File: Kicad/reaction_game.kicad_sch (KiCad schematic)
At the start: 11 parts, among them SW1 Player 1, SW2 Player 2, U1 RaspberryPico

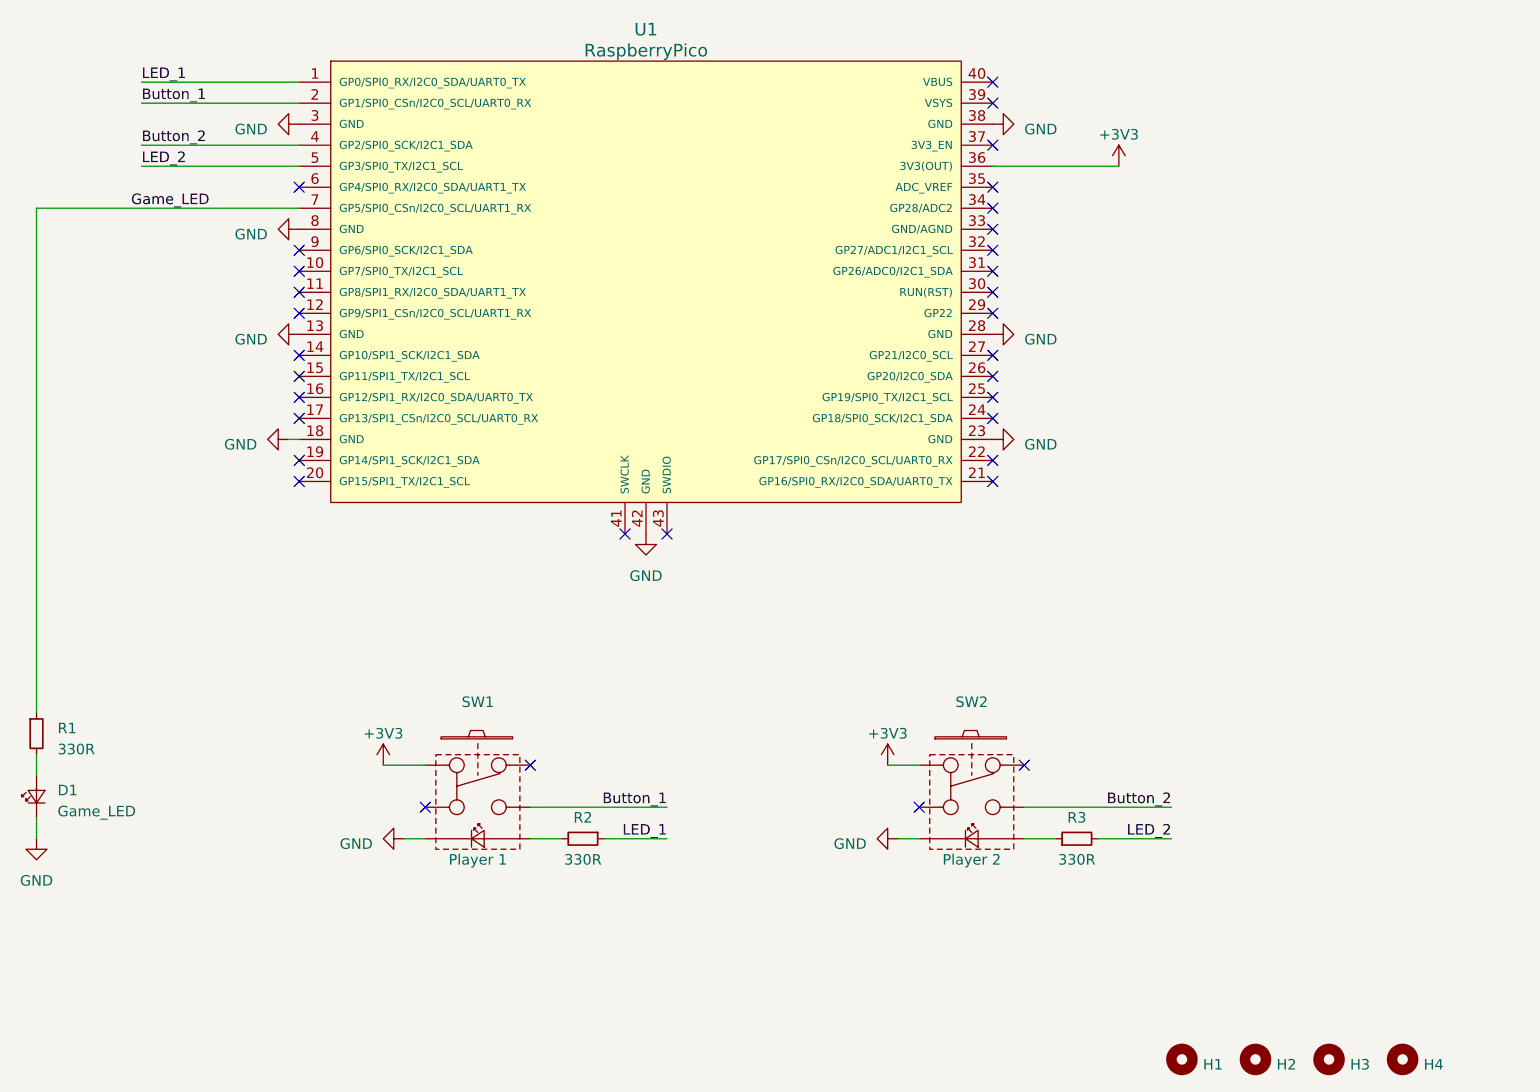
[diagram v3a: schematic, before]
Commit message: Fixed Pico
- flipped pico
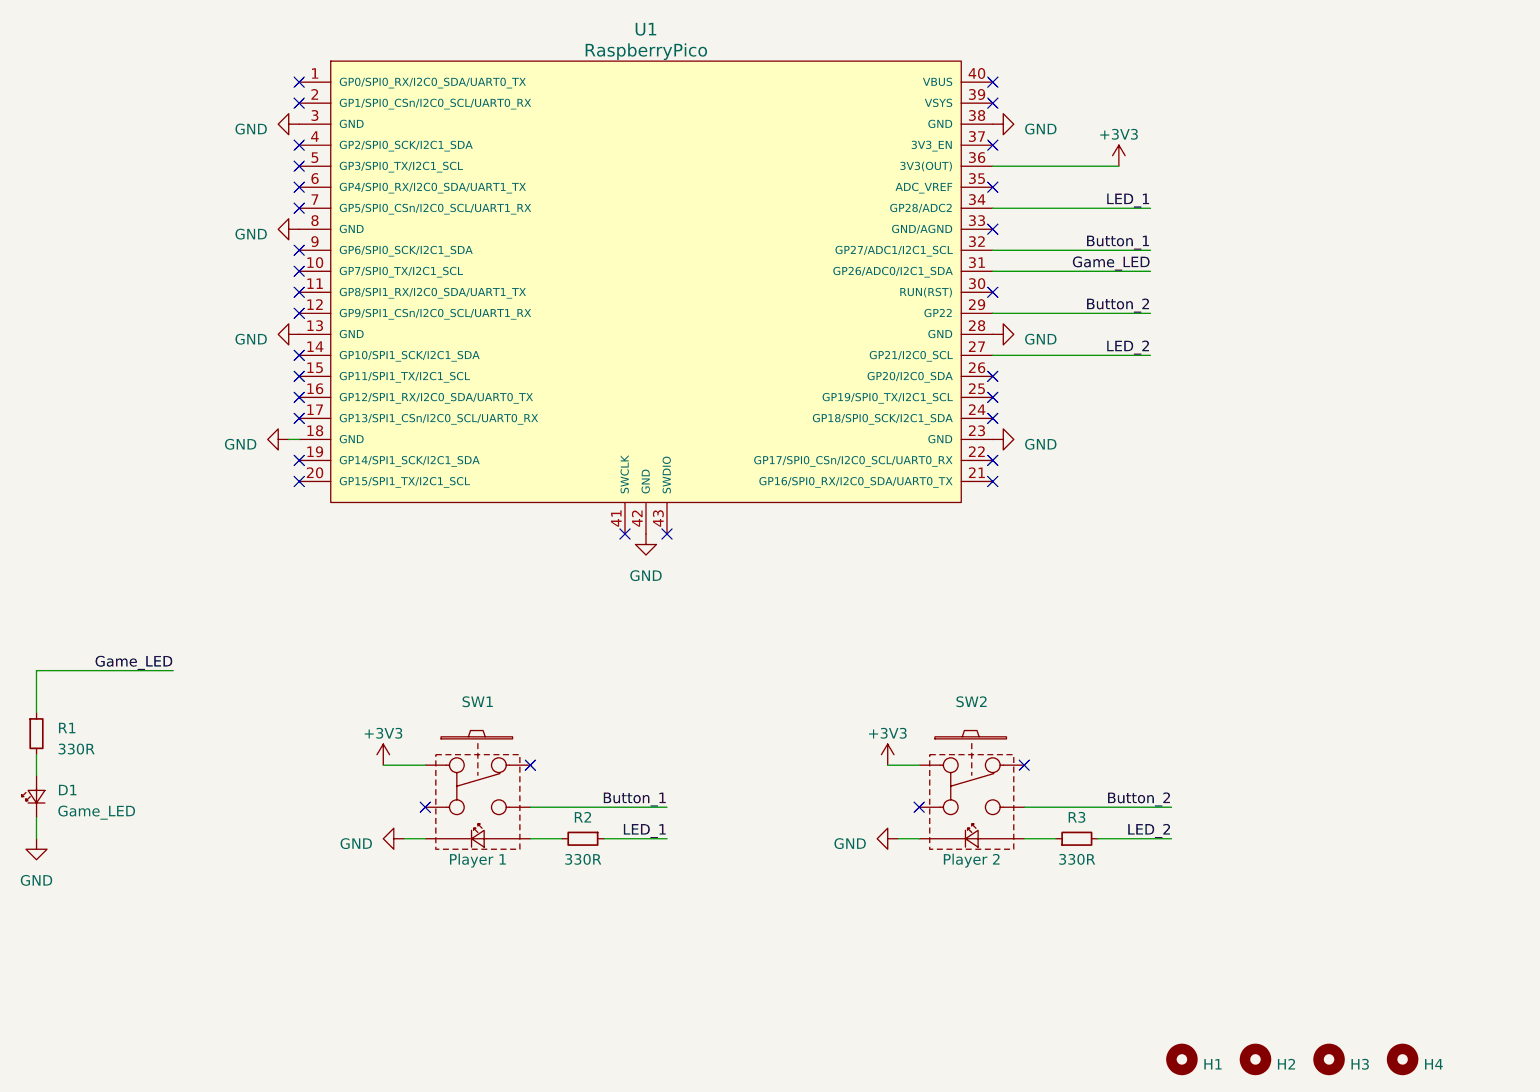
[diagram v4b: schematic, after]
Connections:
- net Button_1: now also U1.32 (GP27/ADC1/I2C1_SCL); no longer U1.2 (GP1/SPI0_CSn/I2C0_SCL/UART0_RX)
- net Button_2: now also U1.29 (GP22); no longer U1.4 (GP2/SPI0_SCK/I2C1_SDA)
- net Game_LED: now also U1.31 (GP26/ADC0/I2C1_SDA); no longer U1.7 (GP5/SPI0_CSn/I2C0_SCL/UART1_RX)
- net LED_1: now also U1.34 (GP28/ADC2); no longer U1.1 (GP0/SPI0_RX/I2C0_SDA/UART0_TX)
- net LED_2: now also U1.27 (GP21/I2C0_SCL); no longer U1.5 (GP3/SPI0_TX/I2C1_SCL)
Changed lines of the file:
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@@
   (no_connect (at 105.41 77.47))
   (no_connect (at 193.04 124.46))
+  (no_connect (at 105.41 44.45))
   (no_connect (at 144.78 96.52))
-  (no_connect (at 189.23 57.15))
   (no_connect (at 105.41 64.77))
   (no_connect (at 105.41 82.55))
-  (no_connect (at 189.23 69.85))
   (no_connect (at 120.65 129.54))
   (no_connect (at 105.41 67.31))
-  (no_connect (at 189.23 62.23))
   (no_connect (at 189.23 87.63))
   (no_connect (at 189.23 80.01))
@@
   (no_connect (at 105.41 74.93))
   (no_connect (at 133.35 124.46))
-  (no_connect (at 189.23 64.77))
   (no_connect (at 105.41 87.63))
   (no_connect (at 189.23 49.53))
+  (no_connect (at 105.41 49.53))
   (no_connect (at 180.34 129.54))
   (no_connect (at 189.23 82.55))
-  (no_connect (at 189.23 74.93))
   (no_connect (at 189.23 90.17))
+  (no_connect (at 105.41 57.15))
   (no_connect (at 189.23 41.91))
+  (no_connect (at 105.41 52.07))
   (no_connect (at 189.23 67.31))
   (no_connect (at 189.23 44.45))
@@
   (no_connect (at 105.41 69.85))
   (no_connect (at 105.41 62.23))
+  (no_connect (at 105.41 41.91))
+  (wire (pts (xy 73.66 113.03) (xy 90.17 113.03))
+    (stroke (width 0) (type default))
+  )
   (wire (pts (xy 201.93 133.35) (xy 210.82 133.35))
     (stroke (width 0) (type default))
@@
     (stroke (width 0) (type default))
   )
-  (wire (pts (xy 86.36 49.53) (xy 105.41 49.53))
+  (wire (pts (xy 208.28 69.85) (xy 189.23 69.85))
     (stroke (width 0) (type default))
   )
@@
     (stroke (width 0) (type default))
   )
+  (wire (pts (xy 73.66 113.03) (xy 73.66 118.11))
+    (stroke (width 0) (type default))
+  )
   (wire (pts (xy 142.24 133.35) (xy 149.86 133.35))
     (stroke (width 0) (type default))
   )
-  (wire (pts (xy 86.36 52.07) (xy 105.41 52.07))
+  (wire (pts (xy 189.23 64.77) (xy 208.28 64.77))
     (stroke (width 0) (type default))
   )
-  (wire (pts (xy 86.36 41.91) (xy 105.41 41.91))
+  (wire (pts (xy 208.28 74.93) (xy 189.23 74.93))
     (stroke (width 0) (type default))
   )
-  (wire (pts (xy 73.66 57.15) (xy 105.41 57.15))
+  (wire (pts (xy 208.28 57.15) (xy 189.23 57.15))
     (stroke (width 0) (type default))
   )
@@
     (stroke (width 0) (type default))
   )
-  (wire (pts (xy 73.66 57.15) (xy 73.66 118.11))
-    (stroke (width 0) (type default))
-  )
   (wire (pts (xy 104.14 85.09) (xy 105.41 85.09))
     (stroke (width 0) (type default))
@@
     (stroke (width 0) (type default))
   )
-  (wire (pts (xy 86.36 44.45) (xy 105.41 44.45))
+  (wire (pts (xy 208.28 62.23) (xy 189.23 62.23))
     (stroke (width 0) (type default))
   )
@@
     (effects (font (size 1.27 1.27)) (justify right bottom))
   )
-  (label "LED_2" (at 86.36 52.07 0) (fields_autoplaced)
-    (effects (font (size 1.27 1.27)) (justify left bottom))
+  (label "Game_LED" (at 208.28 64.77 180) (fields_autoplaced)
+    (effects (font (size 1.27 1.27)) (justify right bottom))
+  )
+  (label "LED_2" (at 208.28 74.93 180) (fields_autoplaced)
+    (effects (font (size 1.27 1.27)) (justify right bottom))
   )
   (label "LED_1" (at 149.86 133.35 180) (fields_autoplaced)
     (effects (font (size 1.27 1.27)) (justify right bottom))
   )
-  (label "Game_LED" (at 85.09 57.15 0) (fields_autoplaced)
-    (effects (font (size 1.27 1.27)) (justify left bottom))
+  (label "Game_LED" (at 90.17 113.03 180) (fields_autoplaced)
+    (effects (font (size 1.27 1.27)) (justify right bottom))
   )
-  (label "Button_1" (at 86.36 44.45 0) (fields_autoplaced)
-    (effects (font (size 1.27 1.27)) (justify left bottom))
+  (label "Button_1" (at 208.28 62.23 180) (fields_autoplaced)
+    (effects (font (size 1.27 1.27)) (justify right bottom))
   )
-  (label "Button_2" (at 86.36 49.53 0) (fields_autoplaced)
-    (effects (font (size 1.27 1.27)) (justify left bottom))
+  (label "Button_2" (at 208.28 69.85 180) (fields_autoplaced)
+    (effects (font (size 1.27 1.27)) (justify right bottom))
   )
-  (label "LED_1" (at 86.36 41.91 0) (fields_autoplaced)
-    (effects (font (size 1.27 1.27)) (justify left bottom))
+  (label "LED_1" (at 208.28 57.15 180) (fields_autoplaced)
+    (effects (font (size 1.27 1.27)) (justify right bottom))
   )
   (symbol (lib_id "MM_Various:MountingHole_NPTH") (at 229.87 160.02 0) (unit 1)

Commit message: Pin change
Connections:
- net Button_2: now also U1.27 (GP21/I2C0_SCL); no longer U1.29 (GP22)
- net LED_2: now also U1.26 (GP20/I2C0_SDA); no longer U1.27 (GP21/I2C0_SCL)
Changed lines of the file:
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@@
   (no_connect (at 120.65 129.54))
   (no_connect (at 105.41 67.31))
+  (no_connect (at 189.23 69.85))
   (no_connect (at 189.23 87.63))
   (no_connect (at 189.23 80.01))
   (no_connect (at 105.41 54.61))
-  (no_connect (at 189.23 77.47))
   (no_connect (at 189.23 59.69))
   (no_connect (at 189.23 54.61))
@@
     (stroke (width 0) (type default))
   )
-  (wire (pts (xy 208.28 69.85) (xy 189.23 69.85))
+  (wire (pts (xy 208.28 77.47) (xy 189.23 77.47))
     (stroke (width 0) (type default))
   )
@@
     (effects (font (size 1.27 1.27)) (justify right bottom))
   )
-  (label "LED_2" (at 208.28 74.93 180) (fields_autoplaced)
+  (label "LED_2" (at 208.28 77.47 180) (fields_autoplaced)
     (effects (font (size 1.27 1.27)) (justify right bottom))
   )
@@
     (effects (font (size 1.27 1.27)) (justify right bottom))
   )
-  (label "Button_2" (at 208.28 69.85 180) (fields_autoplaced)
+  (label "Button_2" (at 208.28 74.93 180) (fields_autoplaced)
     (effects (font (size 1.27 1.27)) (justify right bottom))
   )
